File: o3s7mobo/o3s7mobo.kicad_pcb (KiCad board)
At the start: 2 copper layers, 330 x 217 mm, 30 parts, among them M1541 M1541, M1543 M1543

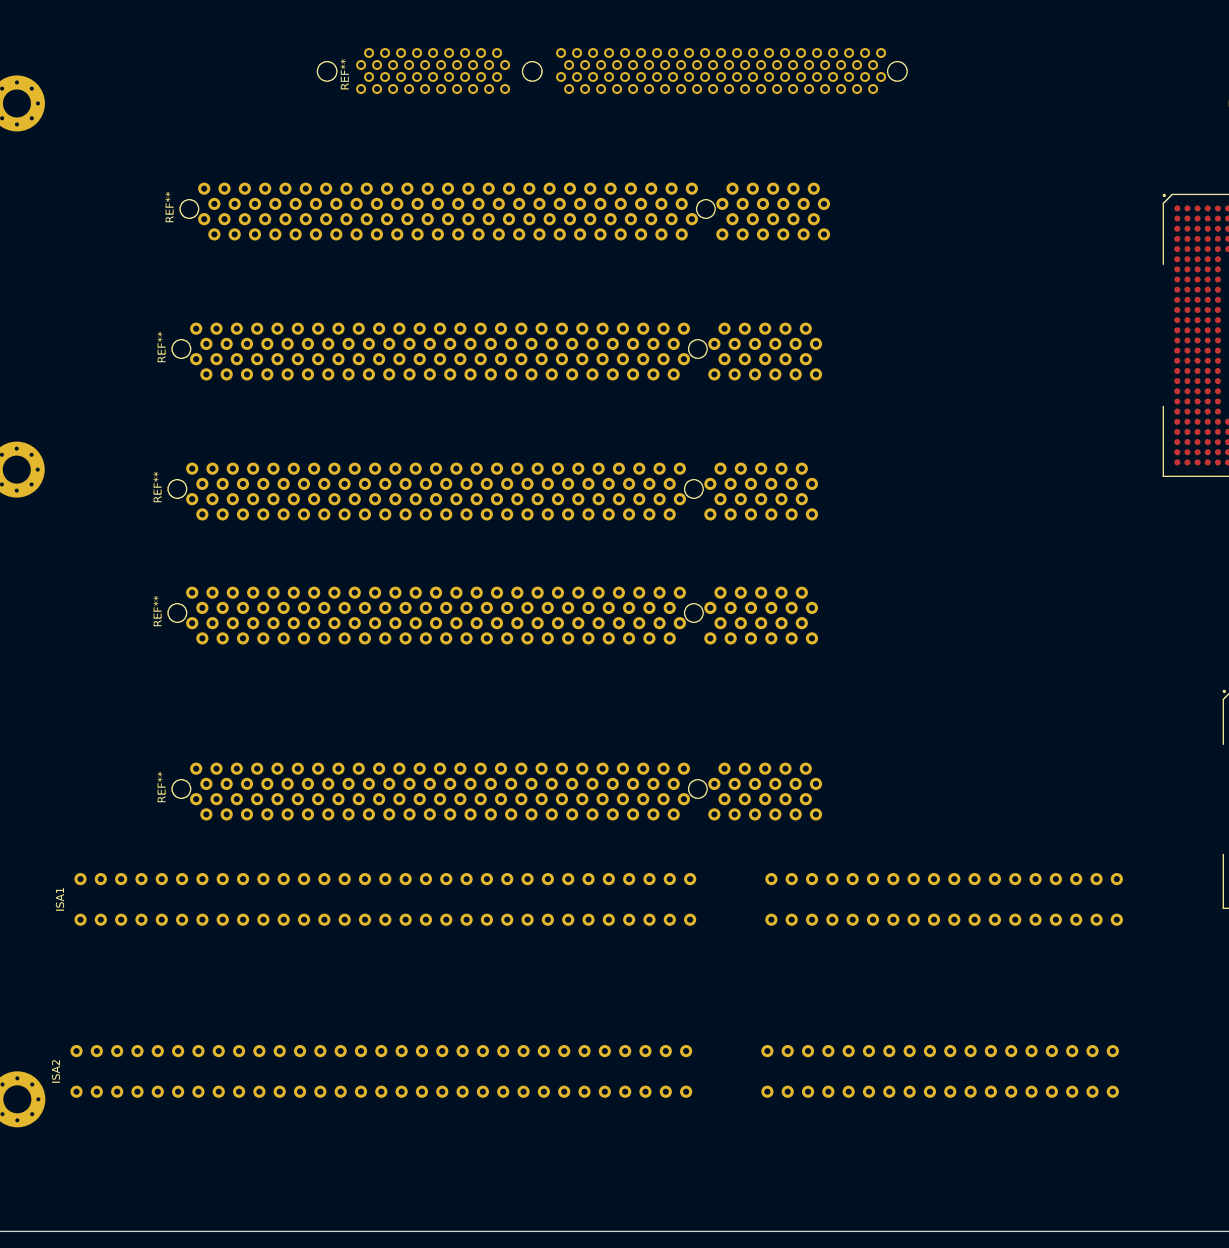
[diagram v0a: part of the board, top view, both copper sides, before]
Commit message: Fixed placement of PCI/ISA/AGP slots
:confetti_ball: :confetti_ball: :confetti_ball:
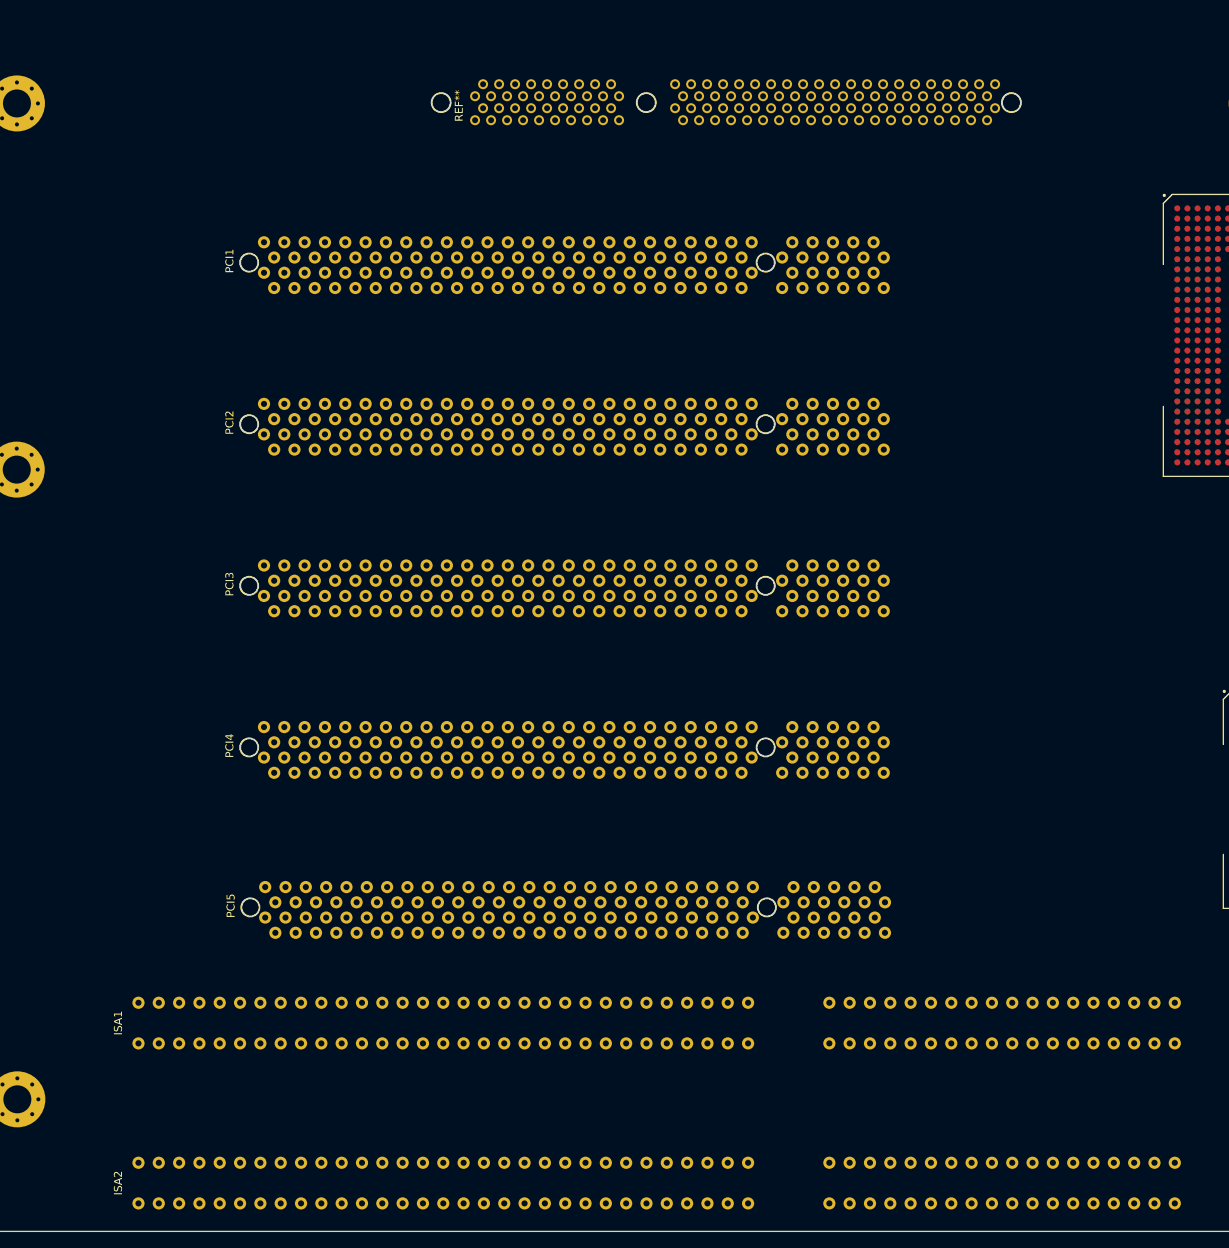
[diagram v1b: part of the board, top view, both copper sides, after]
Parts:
- removed the REF** at (49.0, 110.5)
- removed the REF** at (50.0, 93.0)
- removed the REF** at (48.5, 143.5)
- removed the REF** at (48.5, 128.0)
- added PCI1: PCI, Downloaded:PCI, F.Cu at (57.5, 99.7)
- added PCI2: PCI, Downloaded:PCI, F.Cu at (57.5, 119.9)
- added PCI3: PCI, Downloaded:PCI, F.Cu at (57.5, 140.1)
- added PCI4: PCI, Downloaded:PCI, F.Cu at (57.5, 160.3)
- moved PCI5 17.1 mm to (57.6, 180.3)
- moved ISA1 17.1 mm to (39.2, 190.0)
- moved ISA2 16.0 mm to (39.2, 210.0)
- moved REF** 14.8 mm to (88.8, 74.9)
- renumbered REF** to PCI5
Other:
- outline, holes or cut-outs redrawn

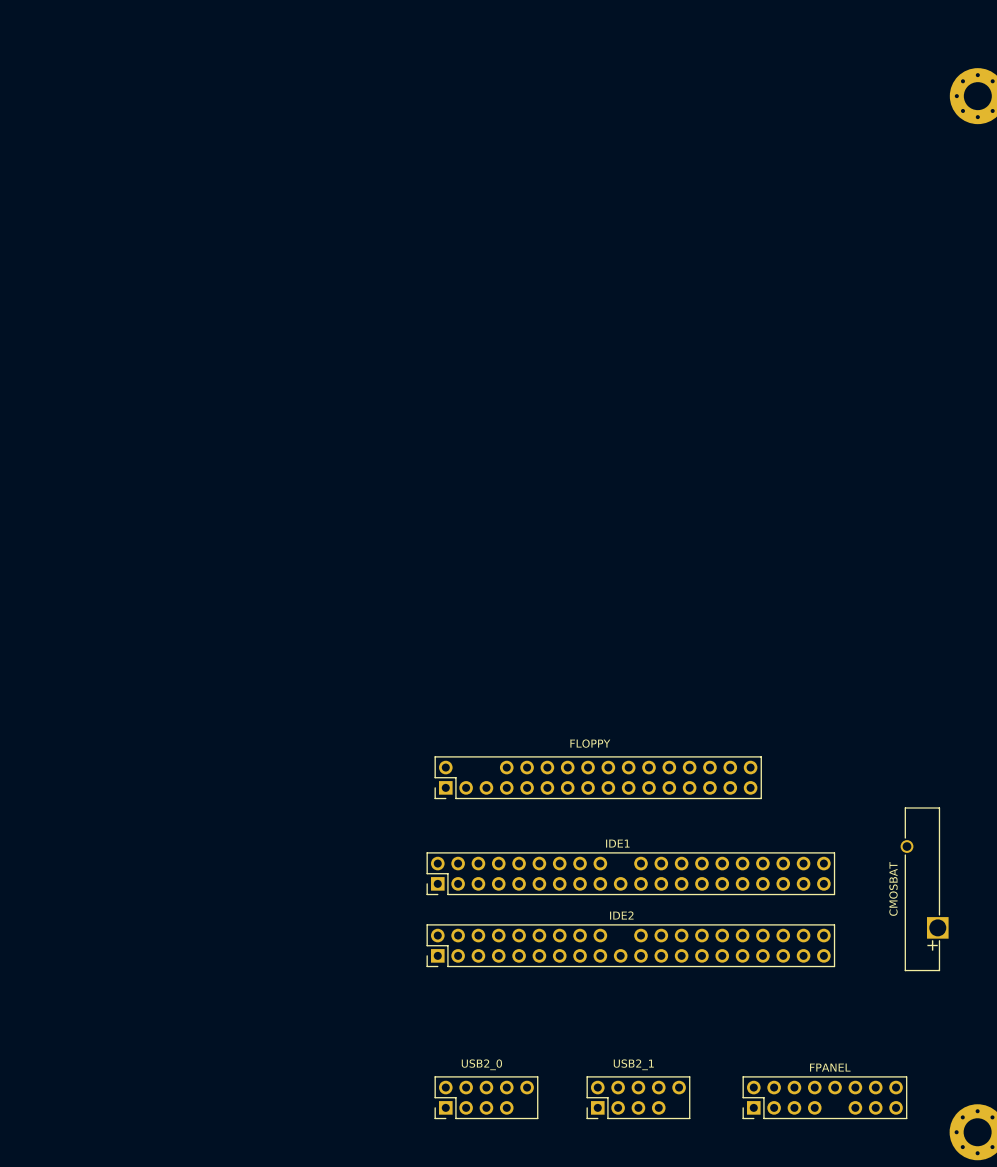
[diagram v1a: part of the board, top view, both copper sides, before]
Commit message: Added socket 7 and AMx holes
Why did it have to have such a jank alphanumeric scheme?

Also, yes, I  fixed the pins the hard way.
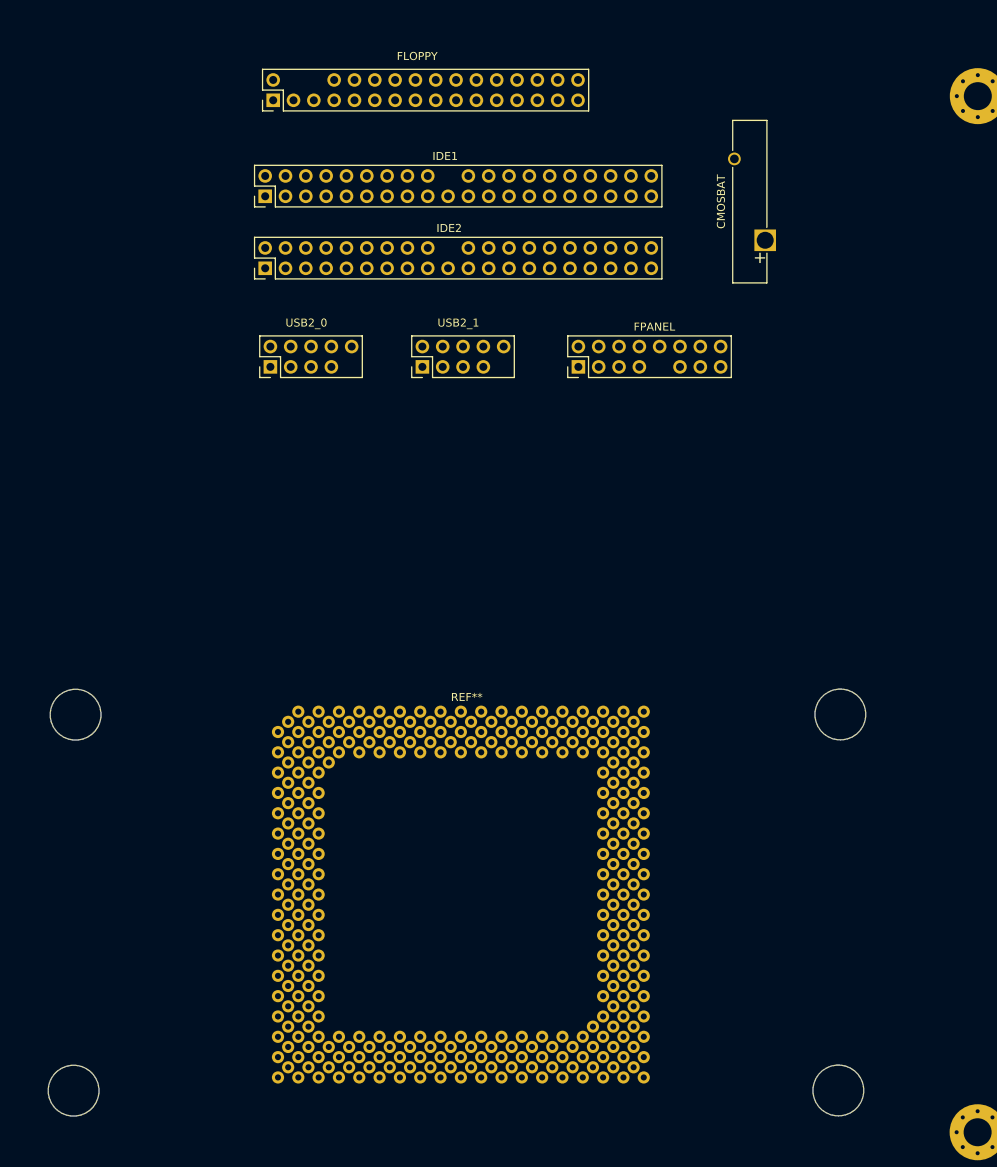
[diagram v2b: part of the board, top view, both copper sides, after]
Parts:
- added REF**: Socket_7, Downloaded:Socket_7, F.Cu at (242.2, 150.2)
- moved FPANEL 95.2 mm to (272.6, 108.9)
- moved USB2_0 95.2 mm to (234.1, 108.9)
- moved USB2_1 95.2 mm to (253.1, 108.9)
- moved CMOSBAT 88.6 mm to (295.9, 93.0)
- moved FLOPPY 88.6 mm to (234.4, 75.5)
- moved IDE1 88.6 mm to (233.4, 87.5)
- moved IDE2 88.6 mm to (233.4, 96.5)
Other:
- outline, holes or cut-outs redrawn

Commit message: Added SDRAM footprints and pads
Just a few things left.
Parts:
- added REF**: SDRAM, Downloaded:SDRAM, F.Cu at (107.7, 17.6)
- added REF**: SDRAM, Downloaded:SDRAM, F.Cu at (107.7, 27.8)
- added REF**: SDRAM, Downloaded:SDRAM, F.Cu at (107.8, 36.6)
- moved ATXFORM 32.0 mm to (9.15, 56.3)
- moved PARALLEL1 32.0 mm to (8.65, 43.3)
- moved SERIAL1 32.0 mm to (10.2, 29.3)
- moved SERIAL2 32.0 mm to (29.1, 29.3)
- moved CMOSBAT 16.9 mm to (290.9, 109.2)
- moved FLOPPY 16.9 mm to (229.4, 91.7)
- moved FPANEL 16.9 mm to (267.5, 125.0)
- moved IDE1 16.9 mm to (228.4, 103.7)
- moved IDE2 16.9 mm to (228.4, 112.7)
- moved USB2_0 16.9 mm to (229.0, 125.0)
- moved USB2_1 16.9 mm to (248.0, 125.0)
- renumbered REF** to Socket7
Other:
- outline, holes or cut-outs redrawn

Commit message: Rearranged components from feedback
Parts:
- moved FLOPPY 128.7 mm to (285.3, 207.6), turned to 180 degrees
- moved IDE1 125.5 mm to (297.3, 208.6), turned to 180 degrees
- moved IDE2 123.6 mm to (306.3, 208.6), turned to 180 degrees
- moved USB2_0 109.4 mm to (323.1, 181.0), turned to 180 degrees
- moved USB2_1 83.7 mm to (323.1, 162.0), turned to 180 degrees
- moved M1543 68.0 mm to (237.7, 187.2)
- moved Socket7 62.3 mm to (223.3, 90.8)
- moved FPANEL 58.2 mm to (323.1, 142.5), turned to 180 degrees
- moved CMOSBAT 32.8 mm to (323.6, 106.7)
- moved ATXFORM 29.8 mm to (38.9, 55.6)
- moved PARALLEL1 29.8 mm to (38.4, 42.6)
- moved SERIAL1 29.8 mm to (39.9, 28.6)
- moved SERIAL2 29.8 mm to (58.9, 28.6)
- moved M1541 22.6 mm to (166.2, 126.1)
- moved REF** 22.6 mm to (87.7, 28.1)
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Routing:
- net (no net): track 0.00 -> 120.6 mm
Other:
- outline, holes or cut-outs redrawn

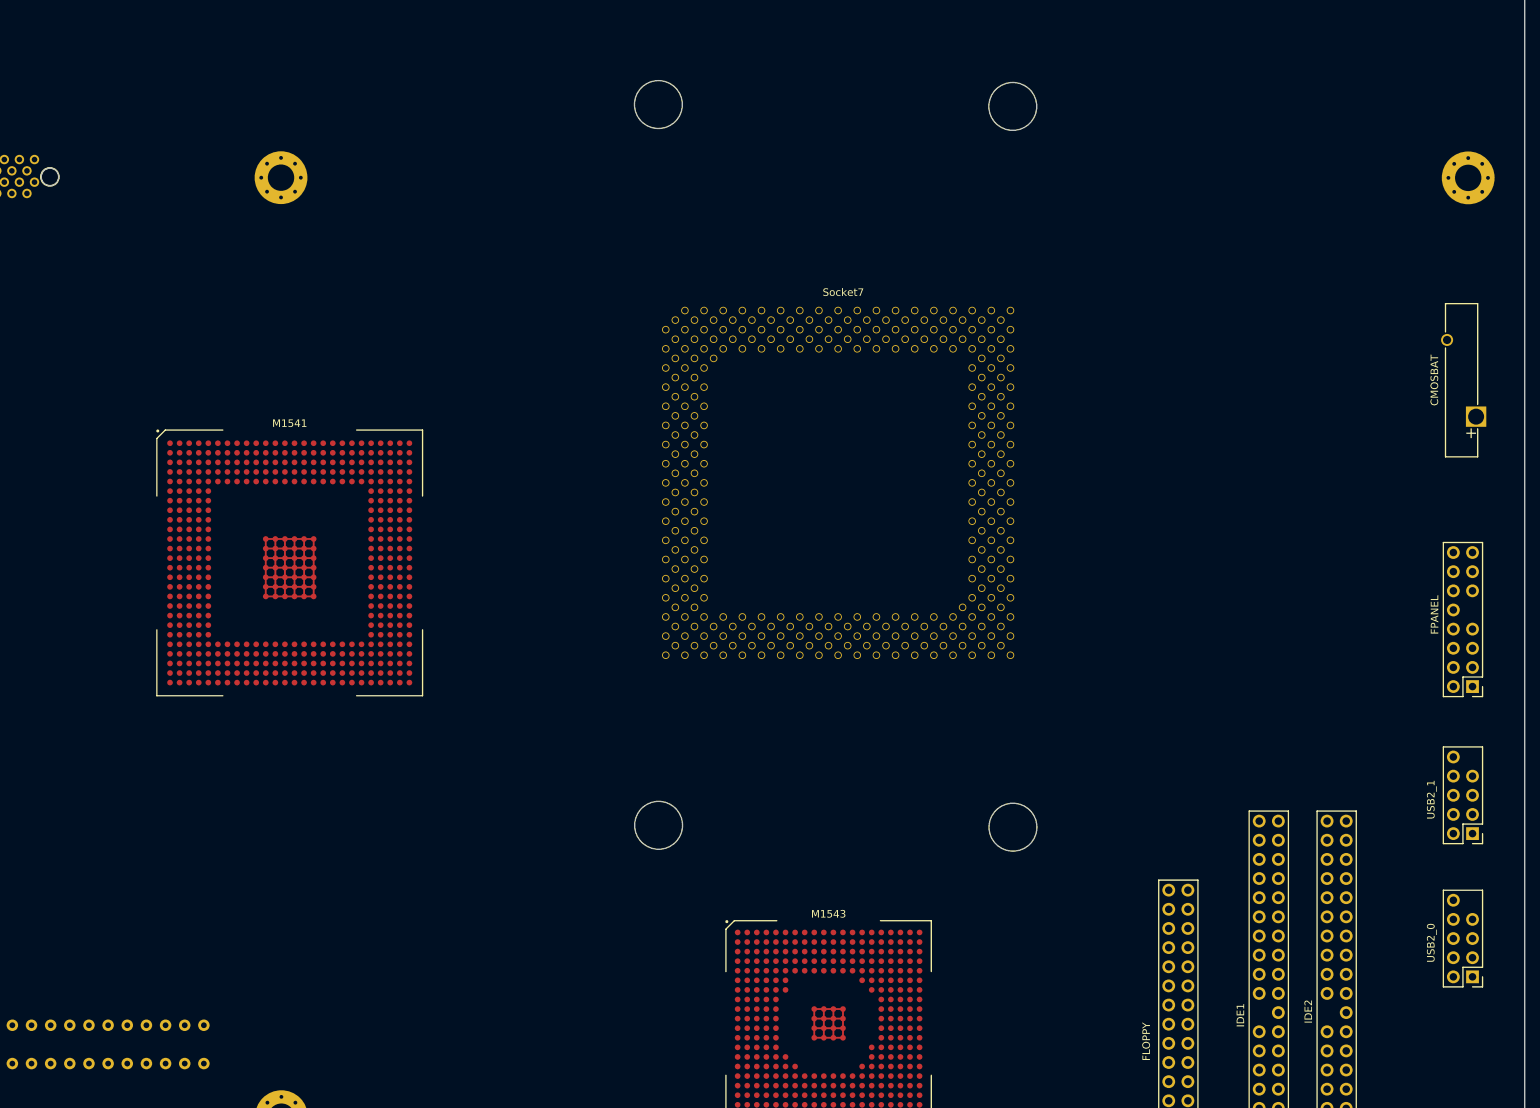
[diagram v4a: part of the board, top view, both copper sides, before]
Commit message: Added SATA footprints and pads
Seems KiCAD's QFP doesn't support rectangular chips yet... making the USB2 going to be a bit trickier.
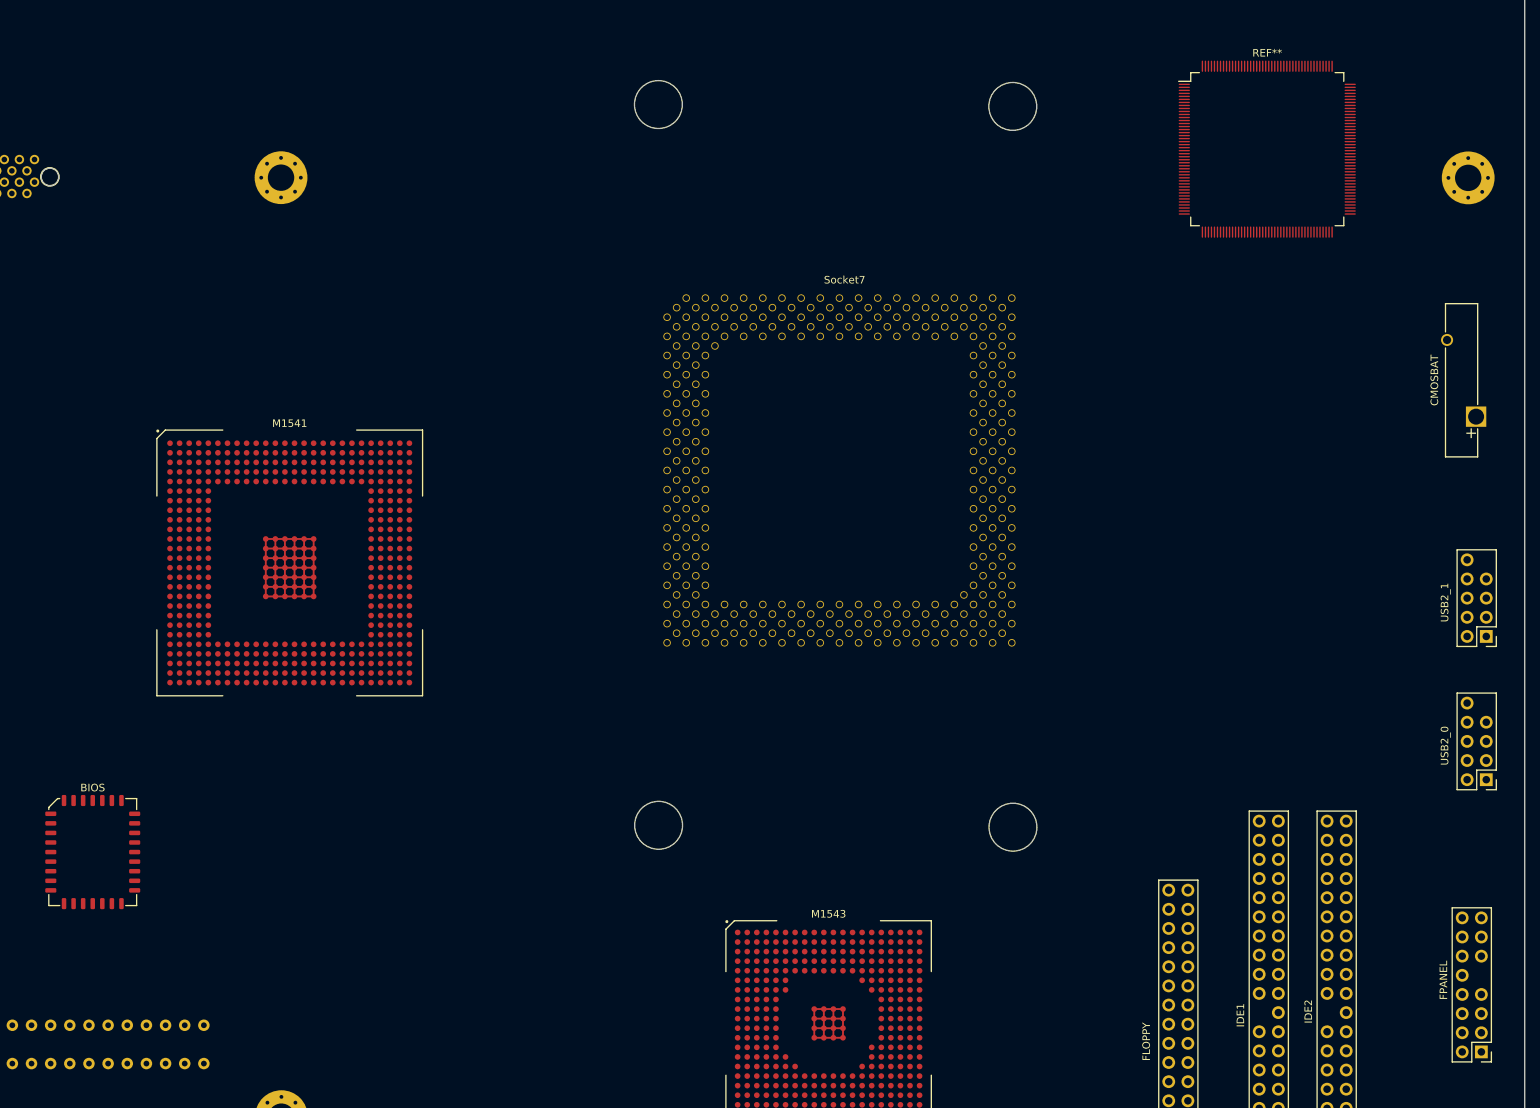
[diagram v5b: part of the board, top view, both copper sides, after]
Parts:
- added BIOS: PLCC-32_11.4x14.0mm_P1.27mm, Package_LCC:PLCC-32_11.4x14.0mm_P1.27mm, F.Cu at (140.1, 164.4)
- added REF**: SiI3114CTU, Downloaded:SiI3114CTU, F.Cu at (295.9, 71.2)
- moved FPANEL 48.5 mm to (324.2, 191.0)
- moved USB2_0 26.2 mm to (324.9, 154.8)
- moved USB2_1 26.2 mm to (324.9, 135.8)
- moved Socket7 1.66 mm to (223.4, 89.2)

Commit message: Added USB2 controller
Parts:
- added REF**: VT6212L, Downloaded:VT6212L, F.Cu at (298.0, 127.2)

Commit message: Added AT power and SATA connectors
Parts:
- added REF**: ATpower, Downloaded:ATpower, F.Cu at (82.7, 4.00)
- added REF**: SATA, Downloaded:SATA, F.Cu at (296.5, 129.2)
- added REF**: SATA, Downloaded:SATA, F.Cu at (296.5, 136.1)
- added REF**: SATA, Downloaded:SATA, F.Cu at (296.5, 142.3)
- added REF**: SATA, Downloaded:SATA, F.Cu at (296.5, 148.8)
- added REF**: ATXpower, Downloaded:ATXpower, F.Cu at (36.0, 5.35)
- moved REF** 40.0 mm to (292.3, 87.7), turned to 90 degrees
- moved REF** 20.6 mm to (293.3, 50.8)
